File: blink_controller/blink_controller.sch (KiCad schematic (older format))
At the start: 13 parts, among them J1 Screw_Terminal_01x02, J2 Screw_Terminal_01x02, Q1 2N2222, U1 NE555P

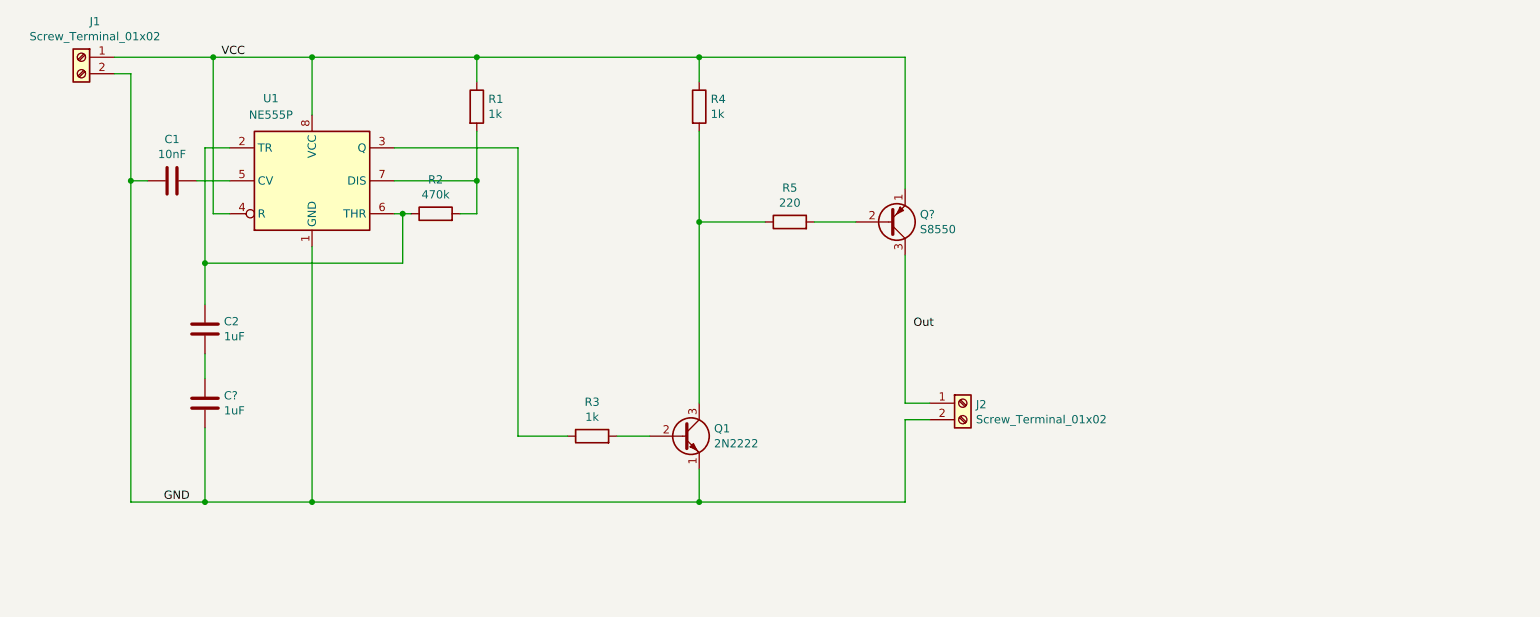
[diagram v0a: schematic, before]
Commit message: Finish schematic
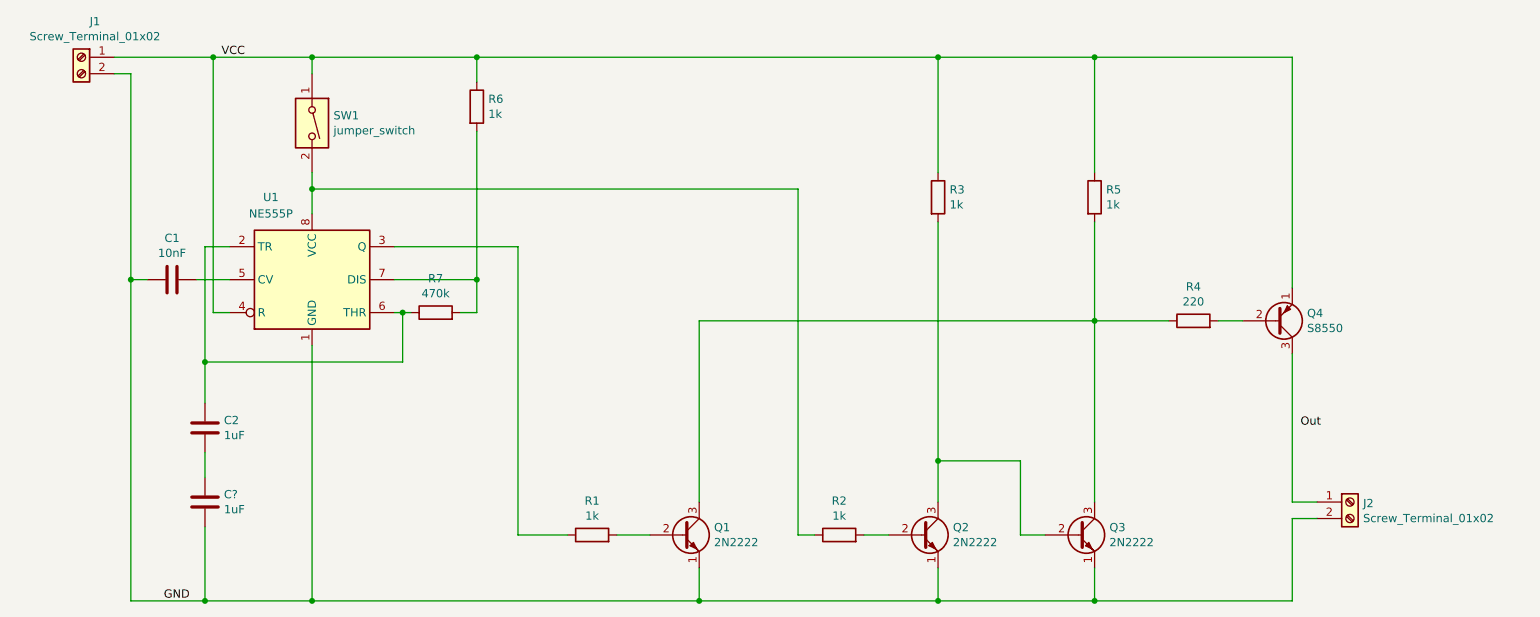
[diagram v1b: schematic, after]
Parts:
- added Q2, Q3: 2N2222, Custom:2N2222_Wide, symbol Custom:2N2222
- added R2, R3: 1k, Resistor_THT:R_Axial_DIN0207_L6.3mm_D2.5mm_P10.16mm_Horizontal, symbol Device:R
- added SW1: jumper_switch, Custom:jumper_switch, symbol Custom:jumper_switch
- gave numbers to parts that had none: 1
- renumbered R3 to R1, R5 to R4, R4 to R5, R1 to R6, R2 to R7
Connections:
- net GND: now also Q2.1 (E), Q3.1 (E)
- net VCC: now also R3.1, SW1.1; no longer U1.8 (VCC)
- net at Q1.3 (C), R4.1, R5.2: now also Q3.3 (C)
- new net: R2.1, SW1.2, U1.8 (VCC)
- new net: Q2.2 (B), R2.2
- new net: Q2.3 (C), Q3.2 (B), R3.2
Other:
- moved on the sheet: C1, C2, C?, J2, Q1, Q4, R1, R4, R5, R7, U1

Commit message: Create PCB
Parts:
- added F1: Fuse, Fuse:Fuseholder_Cylinder-5x20mm_Schurter_0031_8201_Horizontal_Open, symbol Device:Fuse
- C1: footprint (none) -> Capacitor_THT:C_Disc_D5.1mm_W3.2mm_P5.00mm
- gave numbers to parts that had none: 1
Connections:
- net VCC: now also F1.1; no longer J1.1 (Pin_1)
- new net: F1.2, J1.1 (Pin_1)
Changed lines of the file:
@@
 F 0 "C1" V 1298 2250 50  0000 C CNN
 F 1 "10nF" V 1389 2250 50  0000 C CNN
-F 2 "" H 1588 2100 50  0001 C CNN
+F 2 "Capacitor_THT:C_Disc_D5.1mm_W3.2mm_P5.00mm" H 1588 2100 50  0001 C CNN
 F 3 "~" H 1550 2250 50  0001 C CNN
 	1    1550 2250
@@
 $EndComp
 $Comp
-L Device:C C?
+L Device:C C3
 U 1 1 5FD006F6
 P 1750 3600
-F 0 "C?" H 1865 3646 50  0000 L CNN
+F 0 "C3" H 1865 3646 50  0000 L CNN
 F 1 "1uF" H 1865 3555 50  0000 L CNN
 F 2 "Capacitor_THT:CP_Radial_D8.0mm_P3.80mm" H 1788 3450 50  0001 C CNN
@@
 $EndComp
 Wire Wire Line
-	1200 900  1800 900
+	1200 900  1300 900
 Wire Wire Line
 	1300 1000 1300 2250
@@
 Wire Wire Line
 	6200 3350 6200 3600
+$Comp
+L Device:Fuse F1
+U 1 1 5FD7A9BB
+P 1450 900
+F 0 "F1" V 1253 900 50  0000 C CNN
+F 1 "Fuse" V 1344 900 50  0000 C CNN
+F 2 "Fuse:Fuseholder_Cylinder-5x20mm_Schurter_0031_8201_Horizontal_Open" V 1380 900 50  0001 C CNN
+F 3 "~" H 1450 900 50  0001 C CNN
+	1    1450 900
+	0    1    1    0
+$EndComp
+Wire Wire Line
+	1600 900  1800 900
 $EndSCHEMATC
